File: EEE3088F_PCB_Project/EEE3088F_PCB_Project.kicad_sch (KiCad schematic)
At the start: 69 parts, among them IC1 DRV8833PWPR, IC2 DRV8833PWPR, IC3 TPS62067DSGR, IC5 INA219AIDCNR, IC7 TPS61088RHLR, J1 Conn_02x16_Odd_Even, J2 TYPE-C16PIN, J3 Conn_01x02, Q1 AO3400A, Q2 AO3400A, Q5 AO3401A, Q6 AO3401A, SW1 1MS1T1B1M2QES, U1 HUSB237-AA001-DN06R, U2 SLM6600, U3 IRLML6344TRPBF

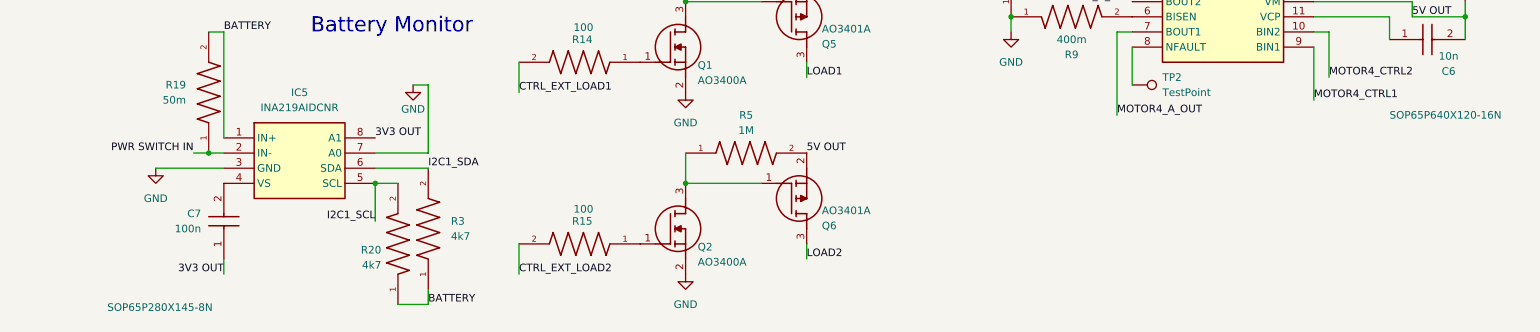
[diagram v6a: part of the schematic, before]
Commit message: v1.2.2
Footprints added
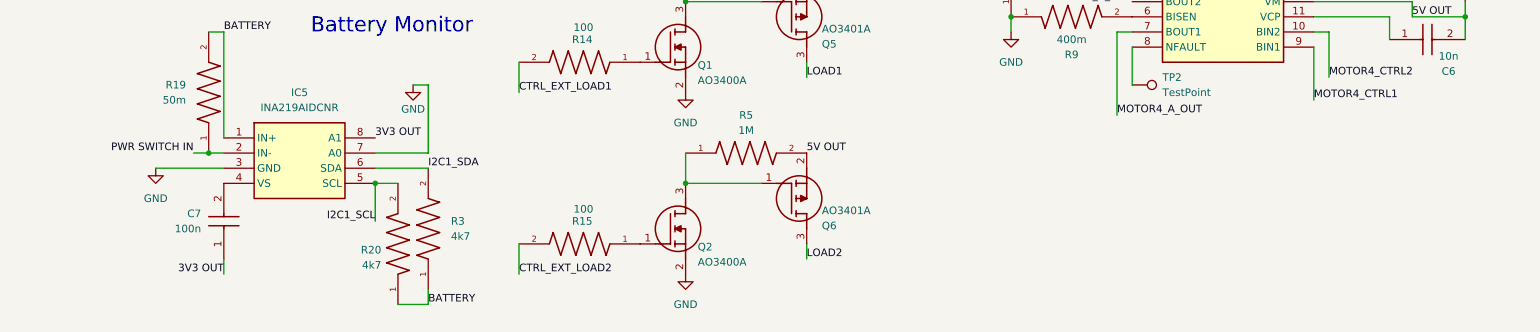
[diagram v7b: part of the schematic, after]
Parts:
- C1: footprint CAPC1608X90N -> CL10C100JB8NNNC KiCad:CAPC1608X90N
- C10, C11, C20, C24, C9: footprint CAPC3216X180N -> CL31A106KBHNNNE KiCad:CAPC3216X180N
- C13, C14, C2: footprint CAPC3216X180N -> CL31B225KBHNNNE KiCad:CAPC3216X180N
- C15: footprint CAPC1608X90N -> CL10B473KB8NNNC KiCad:CAPC1608X90N
- C16: footprint CAPC3215X163N -> 1206B102K202NT KiCad:CAPC3215X163N
- C17, C21, C22: footprint CAPC3216X180N -> CL21A226MAQNNNE KiCad:CAPC2012X140N
- C18, C19, C7: footprint CAPC3216X100N -> CL31B104KBCNNNC KiCad:CAPC3216X100N
- C3: footprint CAPC2012X140N -> CL21A226MAQNNNE KiCad:CAPC2012X140N
- C5, C6: footprint CAPC2012X75N -> CL21B103KBANNNC KiCad:CAPC2012X75N
- IC1, IC2: footprint SOP65P640X120-16N -> DRV8833PWPR KiCad:SOP65P640X120-16N
- IC3: footprint SON50P200X200X80-9N -> TPS62067DSGR KiCad:SON50P200X200X80-9N
- IC5: footprint SOP65P280X145-8N -> INA219AIDCNR KiCad:SOP65P280X145-8N
- IC7: footprint RHL(R-PVQFN-N20)_1 -> TPS61088RHLR KiCad:RHL_R-PVQFN-N20__1
- Q1, Q2: footprint SOT95P280X125-3N -> AO3400A KiCad:SOT95P280X125-3N
- Q5, Q6: footprint SOT95P280X125-3N -> AO3401A KiCad:SOT95P280X125-3N
- U3: footprint IRLML6344TRPBF_INF -> IRLML6344TRPBF:IRLML6344TRPBF_INF
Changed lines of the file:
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@@
 		(polyline
 			(pts
-				(xy 163.83 227.33) (xy 163.83 280.67) (xy 229.87 280.67) (xy 229.87 227.33)
+				(xy 309.245 158.75) (xy 403.86 158.75) (xy 403.86 248.92) (xy 309.245 248.92)
 			)
 			(stroke
@@
 		(polyline
 			(pts
-				(xy 16.3194 217.424) (xy 66.4844 217.424) (xy 66.2305 281.686) (xy 16.0655 281.686)
+				(xy 232.41 212.09) (xy 232.41 280.67) (xy 296.926 280.67) (xy 296.926 212.09)
 			)
 			(stroke
@@
 		(polyline
 			(pts
-				(xy 311.658 154.94) (xy 403.733 155.194) (xy 404.241 15.494) (xy 312.166 15.24)
+				(xy 16.3194 217.424) (xy 66.4844 217.424) (xy 66.2305 281.686) (xy 16.0655 281.686)
 			)
 			(stroke
@@
 		(polyline
 			(pts
-				(xy 232.41 212.09) (xy 232.41 280.67) (xy 296.926 280.67) (xy 296.926 212.09)
+				(xy 311.658 154.94) (xy 403.733 155.194) (xy 404.241 15.494) (xy 312.166 15.24)
 			)
 			(stroke
@@
 		(polyline
 			(pts
-				(xy 309.245 158.75) (xy 403.86 158.75) (xy 403.86 248.92) (xy 309.245 248.92)
+				(xy 163.83 227.33) (xy 163.83 280.67) (xy 229.87 280.67) (xy 229.87 227.33)
 			)
 			(stroke
@@
 			)
 		)
-		(property "Footprint" "CAPC3216X180N"
+		(property "Footprint" "CL31A106KBHNNNE KiCad:CAPC3216X180N"
 			(at 481 133.35 0)
 			(effects
@@
 			)
 		)
-		(property "Footprint" "CAPC3216X180N"
+		(property "Footprint" "CL31A106KBHNNNE KiCad:CAPC3216X180N"
 			(at 120.98 63.5 0)
 			(effects
@@
 			)
 		)
-		(property "Footprint" "RHL(R-PVQFN-N20)_1"
+		(property "Footprint" "TPS61088RHLR KiCad:RHL_R-PVQFN-N20__1"
 			(at 369.57 157.15 0)
 			(effects
@@
 			)
 		)
-		(property "Footprint" "SOP65P640X120-16N"
+		(property "Footprint" "DRV8833PWPR KiCad:SOP65P640X120-16N"
 			(at 364.49 312.09 0)
 			(effects
@@
 			)
 		)
-		(property "Footprint" "CAPC3216X180N"
+		(property "Footprint" "CL31A106KBHNNNE KiCad:CAPC3216X180N"
 			(at 478.46 93.98 0)
 			(effects
@@
 			)
 		)
-		(property "Footprint" "SOT95P280X125-3N"
+		(property "Footprint" "AO3401A KiCad:SOT95P280X125-3N"
 			(at 287.02 128.6 0)
 			(effects
@@
 			)
 		)
-		(property "Footprint" "CAPC1608X90N"
+		(property "Footprint" "CL10C100JB8NNNC KiCad:CAPC1608X90N"
 			(at 237.82 134.62 0)
 			(effects
@@
 			)
 		)
-		(property "Footprint" "CAPC3216X180N"
+		(property "Footprint" "CL31B225KBHNNNE KiCad:CAPC3216X180N"
 			(at 381 317.17 0)
 			(effects
@@
 			)
 		)
-		(property "Footprint" "CAPC3216X180N"
+		(property "Footprint" "CL21A226MAQNNNE KiCad:CAPC2012X140N"
 			(at 386.08 148.26 0)
 			(effects
@@
 			)
 		)
-		(property "Footprint" "SOP65P640X120-16N"
+		(property "Footprint" "DRV8833PWPR KiCad:SOP65P640X120-16N"
 			(at 381 245.618 0)
 			(effects
@@
 				)
 				(justify left top)
+				(hide yes)
 			)
 		)
@@
 			)
 		)
-		(property "Footprint" "SOT95P280X125-3N"
+		(property "Footprint" "AO3400A KiCad:SOT95P280X125-3N"
 			(at 266.7 366.7 0)
 			(effects
@@
 			)
 		)
-		(property "Footprint" "CAPC2012X75N"
+		(property "Footprint" "CL21B103KBANNNC KiCad:CAPC2012X75N"
 			(at 389.89 137.49 0)
 			(effects
@@
 			)
 		)
-		(property "Footprint" "CAPC3216X180N"
+		(property "Footprint" "CL31A106KBHNNNE KiCad:CAPC3216X180N"
 			(at 489.89 218.44 0)
 			(effects
@@
 			)
 		)
-		(property "Footprint" "CAPC3216X180N"
+		(property "Footprint" "CL21A226MAQNNNE KiCad:CAPC2012X140N"
 			(at 386.08 138.1 0)
 			(effects
@@
 			)
 		)
-		(property "Footprint" "CAPC3216X100N"
+		(property "Footprint" "CL31B104KBCNNNC KiCad:CAPC3216X100N"
 			(at 373.38 186.36 0)
 			(effects
@@
 			)
 		)
-		(property "Footprint" "CAPC3216X180N"
+		(property "Footprint" "CL21A226MAQNNNE KiCad:CAPC2012X140N"
 			(at 386.08 127.94 0)
 			(effects
@@
 			)
 		)
-		(property "Footprint" "SOT95P280X125-3N"
+		(property "Footprint" "AO3401A KiCad:SOT95P280X125-3N"
 			(at 287.02 159.08 0)
 			(effects
@@
 			)
 		)
-		(property "Footprint" "CAPC3215X163N"
+		(property "Footprint" "1206B102K202NT KiCad:CAPC3215X163N"
 			(at 346.71 -61.9 0)
 			(effects
@@
 			)
 		)
-		(property "Footprint" "SON50P200X200X80-9N"
+		(property "Footprint" "TPS62067DSGR KiCad:SON50P200X200X80-9N"
 			(at 375.92 219.38 0)
 			(effects
@@
 			)
 		)
-		(property "Footprint" "IRLML6344TRPBF_INF"
+		(property "Footprint" "IRLML6344TRPBF:IRLML6344TRPBF_INF"
 			(at 220.98 138.43 0)
 			(effects
@@
 			)
 		)
-		(property "Footprint" "CAPC3216X100N"
+		(property "Footprint" "CL31B104KBCNNNC KiCad:CAPC3216X100N"
 			(at 89.23 261.62 0)
 			(effects
@@
 			)
 		)
-		(property "Footprint" "CAPC3216X180N"
+		(property "Footprint" "CL31B225KBHNNNE KiCad:CAPC3216X180N"
 			(at 334.01 171.12 0)
 			(effects
@@
 			)
 		)
-		(property "Footprint" "SOT95P280X125-3N"
+		(property "Footprint" "AO3400A KiCad:SOT95P280X125-3N"
 			(at 266.7 336.22 0)
 			(effects
@@
 			)
 		)
-		(property "Footprint" "CAPC1608X90N"
+		(property "Footprint" "CL10B473KB8NNNC KiCad:CAPC1608X90N"
 			(at 377.19 171.12 0)
 			(effects
@@
 			)
 		)
-		(property "Footprint" "CAPC3216X180N"
+		(property "Footprint" "CL31B225KBHNNNE KiCad:CAPC3216X180N"
 			(at 382.27 273.99 0)
 			(effects
@@
 			)
 		)
-		(property "Footprint" "CAPC3216X180N"
+		(property "Footprint" "CL31A106KBHNNNE KiCad:CAPC3216X180N"
 			(at 491.16 175.26 0)
 			(effects
@@
 			)
 		)
-		(property "Footprint" "CAPC2012X140N"
+		(property "Footprint" "CL21A226MAQNNNE KiCad:CAPC2012X140N"
 			(at 237.82 116.84 0)
 			(effects
@@
 			)
 		)
-		(property "Footprint" "CAPC2012X75N"
+		(property "Footprint" "CL21B103KBANNNC KiCad:CAPC2012X75N"
 			(at 391.16 94.31 0)
 			(effects
@@
 			)
 		)
-		(property "Footprint" "CAPC3216X100N"
+		(property "Footprint" "CL31B104KBCNNNC KiCad:CAPC3216X100N"
 			(at 264.49 93.98 0)
 			(effects
@@
 			)
 		)
-		(property "Footprint" "SOP65P280X145-8N"
+		(property "Footprint" "INA219AIDCNR KiCad:SOP65P280X145-8N"
 			(at 165.862 277.876 0)
 			(effects
@@
 				)
 				(justify left top)
+				(hide yes)
 			)
 		)

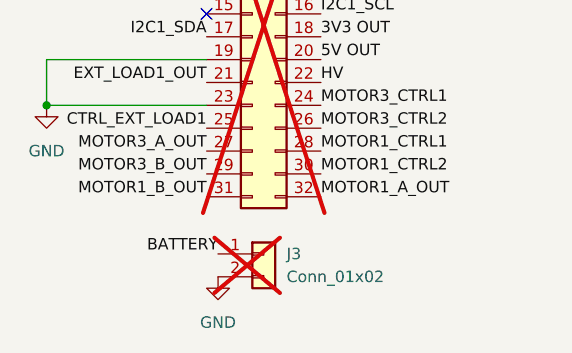
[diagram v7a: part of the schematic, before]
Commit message: v1.3
Lula: all my footprints imported and circuits grouped on PCB
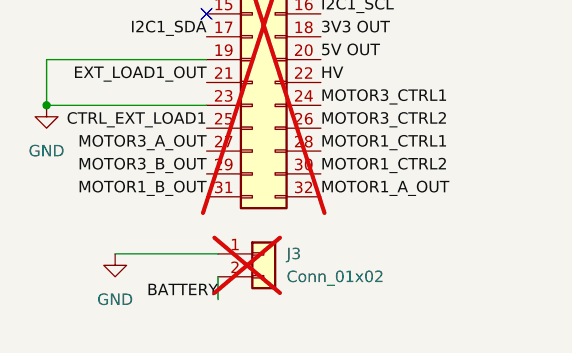
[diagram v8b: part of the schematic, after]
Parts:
- L5: footprint IND_FXL0420_CMT -> FXL0420-1R2-M KiCADv6:IND_FXL0420_CMT
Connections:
- net BATTERY: now also J3.2 (Pin_2); no longer J3.1 (Pin_1)
- net GND: now also J3.1 (Pin_1); no longer J3.2 (Pin_2)
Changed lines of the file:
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@@
 	(wire
 		(pts
+			(xy 26.67 271.78) (xy 38.1 271.78)
+		)
+		(stroke
+			(width 0)
+			(type default)
+		)
+	)
+	(wire
+		(pts
 			(xy 369.57 163.83) (xy 369.57 173.99)
 		)
@@
 	(wire
 		(pts
+			(xy 38.1 274.32) (xy 38.1 276.86)
+		)
+		(stroke
+			(width 0)
+			(type default)
+		)
+	)
+	(wire
+		(pts
 			(xy 349.25 132.08) (xy 344.17 132.08)
 		)
@@
 	)
 	(label "BATTERY"
-		(at 38.1 271.78 180)
+		(at 38.1 276.86 180)
 		(effects
 			(font
@@
 		(polyline
 			(pts
-				(xy 232.41 212.09) (xy 232.41 280.67) (xy 296.926 280.67) (xy 296.926 212.09)
+				(xy 163.83 227.33) (xy 163.83 280.67) (xy 229.87 280.67) (xy 229.87 227.33)
 			)
 			(stroke
@@
 		(polyline
 			(pts
-				(xy 16.3194 217.424) (xy 66.4844 217.424) (xy 66.2305 281.686) (xy 16.0655 281.686)
+				(xy 232.41 212.09) (xy 232.41 280.67) (xy 296.926 280.67) (xy 296.926 212.09)
 			)
 			(stroke
@@
 		(polyline
 			(pts
-				(xy 163.83 227.33) (xy 163.83 280.67) (xy 229.87 280.67) (xy 229.87 227.33)
+				(xy 16.3194 217.424) (xy 66.4844 217.424) (xy 66.2305 281.686) (xy 16.0655 281.686)
 			)
 			(stroke
@@
 			)
 		)
-		(property "Footprint" "IND_FXL0420_CMT"
+		(property "Footprint" "FXL0420-1R2-M KiCADv6:IND_FXL0420_CMT"
 			(at 334.01 127 0)
 			(effects
@@
 	(symbol
 		(lib_id "power:GND")
-		(at 38.1 274.32 0)
+		(at 26.67 271.78 0)
 		(unit 1)
 		(exclude_from_sim no)
@@
 		(fields_autoplaced yes)
 		(property "Reference" "#PWR014"
-			(at 38.1 280.67 0)
+			(at 26.67 278.13 0)
 			(effects
 				(font
@@
 		)
 		(property "Value" "GND"
-			(at 38.1 279.4 0)
+			(at 26.67 276.86 0)
 			(effects
 				(font
@@
 		)
 		(property "Footprint" ""
-			(at 38.1 274.32 0)
+			(at 26.67 271.78 0)
 			(effects
 				(font
@@
 		)
 		(property "Datasheet" ""
-			(at 38.1 274.32 0)
+			(at 26.67 271.78 0)
 			(effects
 				(font
@@
 		)
 		(property "Description" "Power symbol creates a global label with name \"GND\" , ground"
-			(at 38.1 274.32 0)
+			(at 26.67 271.78 0)
 			(effects
 				(font
